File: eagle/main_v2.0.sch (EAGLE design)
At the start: 97 parts, among them IC1 74HC257D, IC2 PCA9530, IC3 RAC04, IC4 CS8416, IC5 MCP130-300I/SN, IC6 MAX1724, K1 G6A-234P, T1 BC847, T2 BC857, T3 BC847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

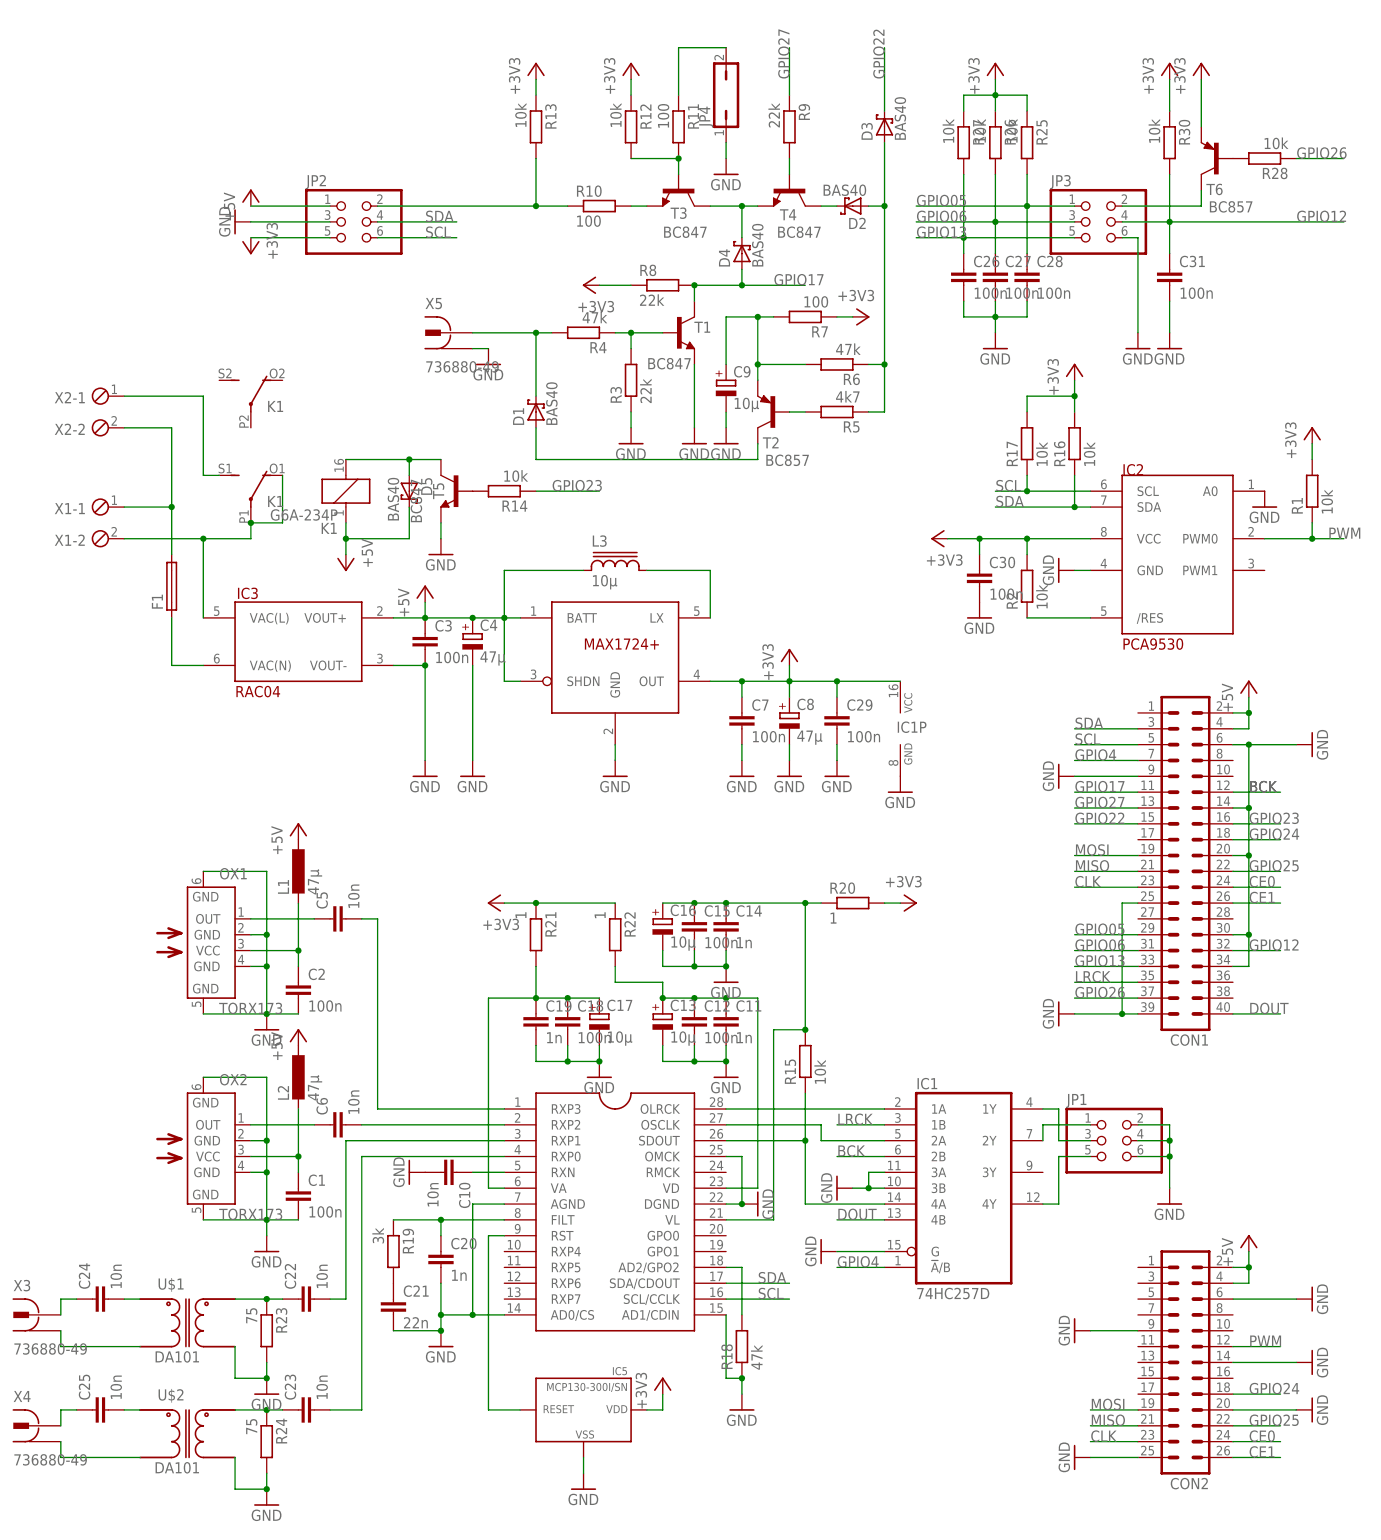
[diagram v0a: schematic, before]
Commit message: Eagle-Files: V2.0, zusätzlichen Ausgang für Relais eingebaut
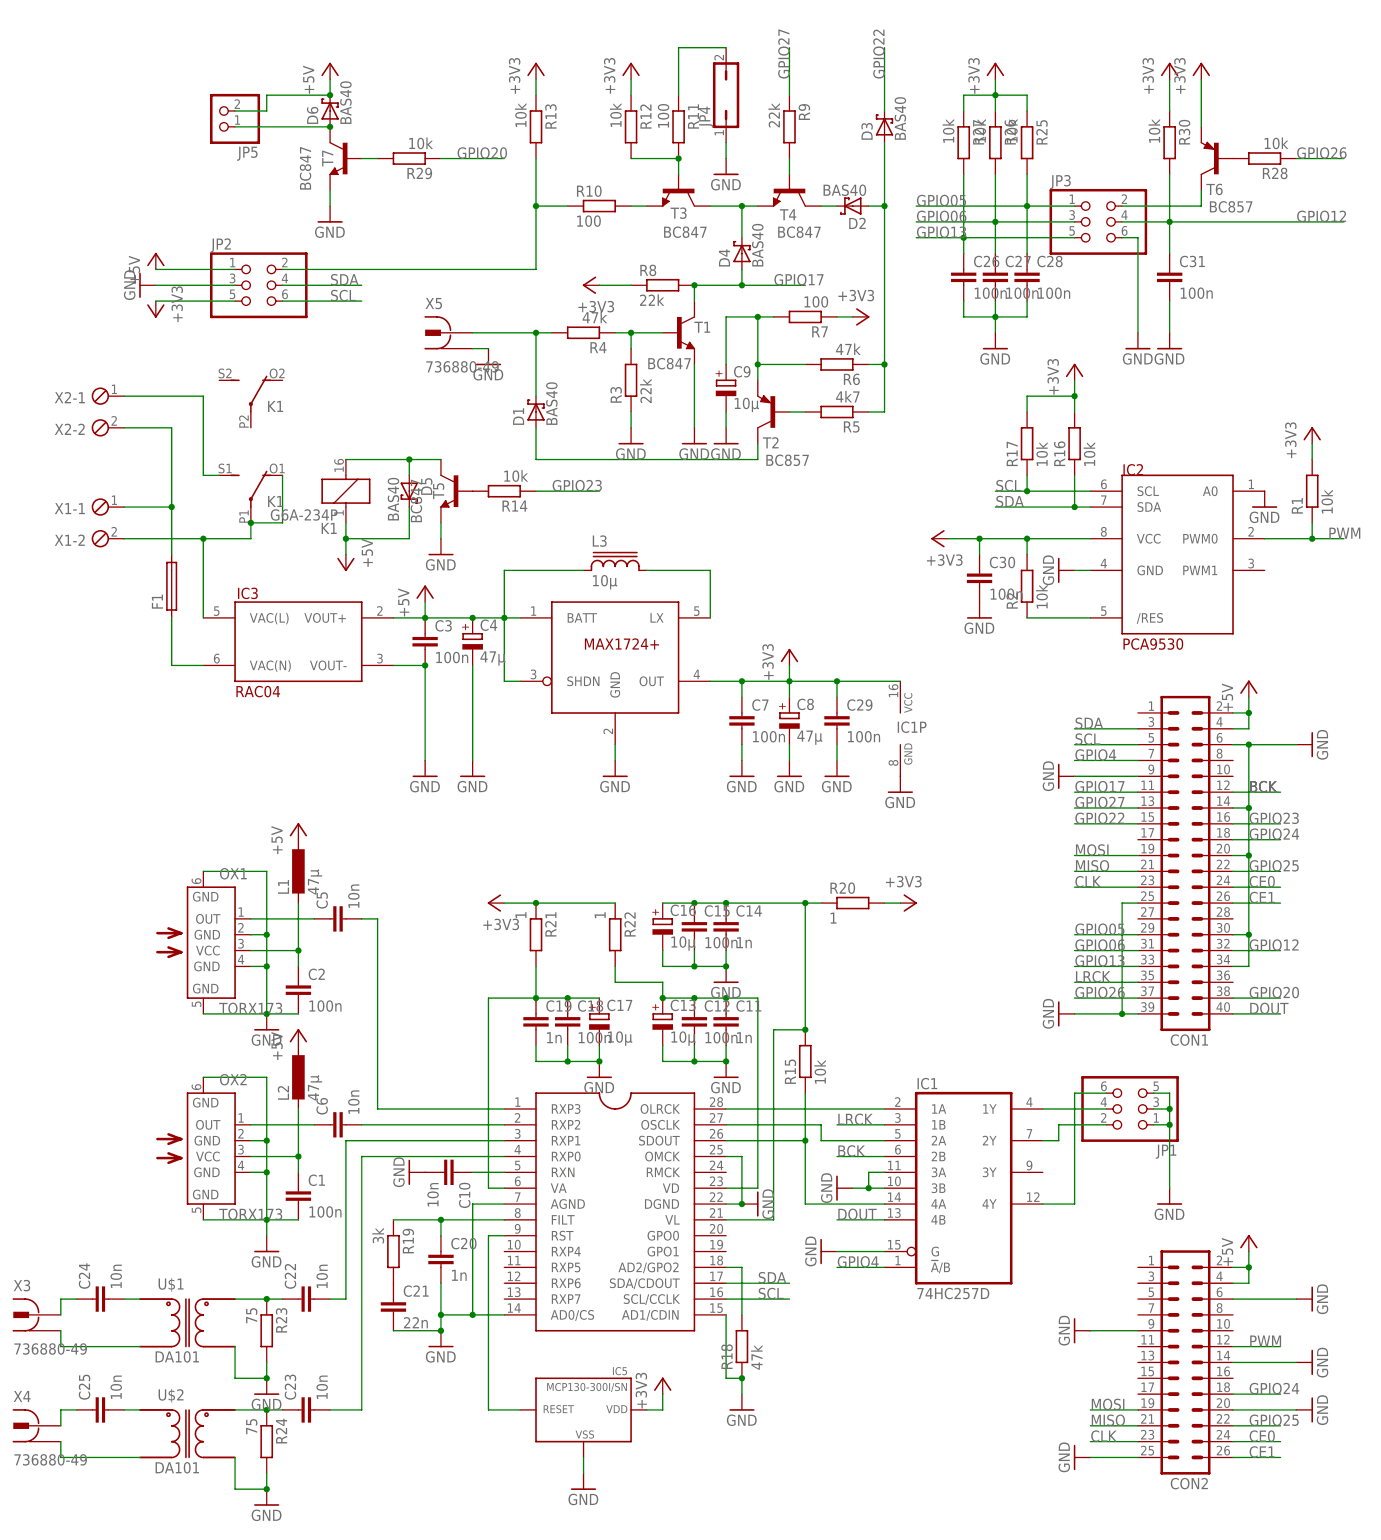
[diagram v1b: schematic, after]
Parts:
- added D6: BAS40, diode:BAS40
- added JP5: (no value), pinhead:PINHD-1X2
- added R29: 10k, rcl:R-EU_R0805
- added T7: BC847, transistor:BC847-NPN-SOT23-BEC
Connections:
- new net GPIO20: CON1.38, R29.1
- new net N$52: D6.A, JP5.1, T7.C
- new net N$55: R29.2, T7.B
- net +5V: now also D6.C, JP5.2
- net GND: now also JP1.1, JP1.3, JP1.5, T7.E; no longer JP1.2, JP1.4, JP1.6
- net N$26: now also JP1.2; no longer JP1.1
- net N$27: now also JP1.4; no longer JP1.3
- net N$53: now also JP1.6; no longer JP1.5
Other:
- moved on the sheet: JP1, JP2
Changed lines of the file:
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@@
 <part name="X5" library="con-conrad" deviceset="736880-49" device=""/>
 <part name="+3V15" library="supply1" deviceset="+3V3" device=""/>
+<part name="D6" library="diode" deviceset="BAS40" device=""/>
+<part name="T7" library="transistor" deviceset="*-NPN-" device="SOT23-BEC" technology="BC847" value="BC847"/>
+<part name="R29" library="rcl" deviceset="R-EU_" device="R0805" value="10k"/>
+<part name="GND44" library="supply1" deviceset="GND" device=""/>
+<part name="P+4" library="supply1" deviceset="+5V" device=""/>
+<part name="JP5" library="pinhead" deviceset="PINHD-1X2" device=""/>
 </parts>
 <sheets>
@@
 <attribute name="VALUE" x="88.9" y="172.72" size="1.778" layer="96"/>
 </instance>
-<instance part="JP1" gate="A" x="152.4" y="63.5"/>
+<instance part="JP1" gate="A" x="157.48" y="68.58" rot="R180"/>
 <instance part="GND15" gate="1" x="162.56" y="53.34"/>
 <instance part="T5" gate="G$1" x="48.26" y="167.64" smashed="yes" rot="MR0">
@@
 <instance part="F1" gate="F" x="2.54" y="152.4" rot="R90"/>
 <instance part="GND32" gate="1" x="53.34" y="187.96"/>
-<instance part="JP2" gate="A" x="30.48" y="210.82"/>
+<instance part="JP2" gate="A" x="15.24" y="200.66"/>
 <instance part="JP3" gate="A" x="149.86" y="210.82"/>
-<instance part="GND33" gate="1" x="12.7" y="210.82" rot="R270"/>
-<instance part="P+12" gate="1" x="15.24" y="215.9"/>
-<instance part="+3V7" gate="G$1" x="15.24" y="205.74" rot="R180"/>
+<instance part="GND33" gate="1" x="-2.54" y="200.66" rot="R270"/>
+<instance part="P+12" gate="1" x="0" y="205.74"/>
+<instance part="+3V7" gate="G$1" x="0" y="195.58" rot="R180"/>
 <instance part="GND34" gate="1" x="157.48" y="190.5"/>
 <instance part="R25" gate="G$1" x="139.7" y="223.52" rot="R270"/>
@@
 <instance part="X5" gate="G$1" x="48.26" y="193.04"/>
 <instance part="+3V15" gate="G$1" x="121.92" y="101.6" rot="R270"/>
+<instance part="D6" gate="1" x="27.94" y="228.6" rot="R90"/>
+<instance part="T7" gate="G$1" x="30.48" y="220.98" smashed="yes" rot="MR0">
+<attribute name="NAME" x="26.67" y="219.71" size="1.778" layer="95" rot="MR90"/>
+<attribute name="VALUE" x="24.892" y="223.012" size="1.778" layer="96" rot="MR270"/>
+</instance>
+<instance part="R29" gate="G$1" x="40.64" y="220.98" rot="R180"/>
+<instance part="GND44" gate="1" x="27.94" y="210.82"/>
+<instance part="P+4" gate="1" x="27.94" y="236.22"/>
+<instance part="JP5" gate="G$1" x="10.16" y="228.6" rot="R180"/>
 </instances>
 <busses>
@@
 <segment>
 <pinref part="JP2" gate="A" pin="4"/>
-<wire x1="35.56" y1="210.82" x2="48.26" y2="210.82" width="0.1524" layer="91"/>
-<label x="43.18" y="210.82" size="1.778" layer="95"/>
+<wire x1="20.32" y1="200.66" x2="33.02" y2="200.66" width="0.1524" layer="91"/>
+<label x="27.94" y="200.66" size="1.778" layer="95"/>
 </segment>
 </net>
@@
 <segment>
 <pinref part="JP2" gate="A" pin="6"/>
-<wire x1="35.56" y1="208.28" x2="48.26" y2="208.28" width="0.1524" layer="91"/>
-<label x="43.18" y="208.28" size="1.778" layer="95"/>
+<wire x1="20.32" y1="198.12" x2="33.02" y2="198.12" width="0.1524" layer="91"/>
+<label x="27.94" y="198.12" size="1.778" layer="95"/>
 </segment>
 </net>
@@
 </segment>
 <segment>
-<pinref part="JP1" gate="A" pin="2"/>
-<wire x1="157.48" y1="66.04" x2="162.56" y2="66.04" width="0.1524" layer="91"/>
-<wire x1="162.56" y1="66.04" x2="162.56" y2="63.5" width="0.1524" layer="91"/>
 <pinref part="GND15" gate="1" pin="GND"/>
-<pinref part="JP1" gate="A" pin="4"/>
-<wire x1="162.56" y1="63.5" x2="162.56" y2="60.96" width="0.1524" layer="91"/>
-<wire x1="162.56" y1="60.96" x2="162.56" y2="55.88" width="0.1524" layer="91"/>
-<wire x1="157.48" y1="63.5" x2="162.56" y2="63.5" width="0.1524" layer="91"/>
-<junction x="162.56" y="63.5"/>
-<pinref part="JP1" gate="A" pin="6"/>
-<wire x1="157.48" y1="60.96" x2="162.56" y2="60.96" width="0.1524" layer="91"/>
-<junction x="162.56" y="60.96"/>
+<pinref part="JP1" gate="A" pin="1"/>
+<pinref part="JP1" gate="A" pin="5"/>
+<wire x1="160.02" y1="71.12" x2="162.56" y2="71.12" width="0.1524" layer="91"/>
+<wire x1="162.56" y1="71.12" x2="162.56" y2="68.58" width="0.1524" layer="91"/>
+<pinref part="JP1" gate="A" pin="3"/>
+<wire x1="162.56" y1="68.58" x2="160.02" y2="68.58" width="0.1524" layer="91"/>
+<wire x1="162.56" y1="68.58" x2="162.56" y2="66.04" width="0.1524" layer="91"/>
+<junction x="162.56" y="68.58"/>
+<wire x1="162.56" y1="66.04" x2="160.02" y2="66.04" width="0.1524" layer="91"/>
+<wire x1="162.56" y1="66.04" x2="162.56" y2="55.88" width="0.1524" layer="91"/>
+<junction x="162.56" y="66.04"/>
 </segment>
 <segment>
@@
 <segment>
 <pinref part="JP2" gate="A" pin="3"/>
-<wire x1="27.94" y1="210.82" x2="15.24" y2="210.82" width="0.1524" layer="91"/>
+<wire x1="12.7" y1="200.66" x2="0" y2="200.66" width="0.1524" layer="91"/>
 <pinref part="GND33" gate="1" pin="GND"/>
 </segment>
@@
 <pinref part="CON2" gate="G$1" pin="25"/>
 <wire x1="149.86" y1="12.7" x2="157.48" y2="12.7" width="0.1524" layer="91"/>
+</segment>
+<segment>
+<pinref part="GND44" gate="1" pin="GND"/>
+<pinref part="T7" gate="G$1" pin="E"/>
+<wire x1="27.94" y1="213.36" x2="27.94" y2="215.9" width="0.1524" layer="91"/>
 </segment>
 </net>
@@
 <pinref part="P+12" gate="1" pin="+5V"/>
 <pinref part="JP2" gate="A" pin="1"/>
-<wire x1="15.24" y1="213.36" x2="27.94" y2="213.36" width="0.1524" layer="91"/>
+<wire x1="0" y1="203.2" x2="12.7" y2="203.2" width="0.1524" layer="91"/>
+</segment>
+<segment>
+<pinref part="D6" gate="1" pin="C"/>
+<pinref part="P+4" gate="1" pin="+5V"/>
+<wire x1="27.94" y1="231.14" x2="27.94" y2="233.68" width="0.1524" layer="91"/>
+<pinref part="JP5" gate="G$1" pin="2"/>
+<wire x1="12.7" y1="228.6" x2="17.78" y2="228.6" width="0.1524" layer="91"/>
+<wire x1="17.78" y1="228.6" x2="17.78" y2="231.14" width="0.1524" layer="91"/>
+<wire x1="17.78" y1="231.14" x2="27.94" y2="231.14" width="0.1524" layer="91"/>
+<junction x="27.94" y="231.14"/>
 </segment>
 </net>
@@
 <segment>
 <pinref part="JP2" gate="A" pin="5"/>
-<wire x1="27.94" y1="208.28" x2="15.24" y2="208.28" width="0.1524" layer="91"/>
+<wire x1="12.7" y1="198.12" x2="0" y2="198.12" width="0.1524" layer="91"/>
 <pinref part="+3V7" gate="G$1" pin="+3V3"/>
 </segment>
@@
 <wire x1="60.96" y1="213.36" x2="66.04" y2="213.36" width="0.1524" layer="91"/>
 <pinref part="JP2" gate="A" pin="2"/>
-<wire x1="35.56" y1="213.36" x2="60.96" y2="213.36" width="0.1524" layer="91"/>
 <junction x="60.96" y="213.36"/>
+<wire x1="60.96" y1="213.36" x2="60.96" y2="203.2" width="0.1524" layer="91"/>
+<wire x1="60.96" y1="203.2" x2="20.32" y2="203.2" width="0.1524" layer="91"/>
 </segment>
 </net>
@@
 <segment>
 <pinref part="IC1" gate="A" pin="2Y"/>
-<wire x1="142.24" y1="63.5" x2="142.24" y2="66.04" width="0.1524" layer="91"/>
-<pinref part="JP1" gate="A" pin="1"/>
-<wire x1="142.24" y1="66.04" x2="149.86" y2="66.04" width="0.1524" layer="91"/>
+<pinref part="JP1" gate="A" pin="2"/>
+<wire x1="144.78" y1="66.04" x2="152.4" y2="66.04" width="0.1524" layer="91"/>
+<wire x1="144.78" y1="66.04" x2="144.78" y2="63.5" width="0.1524" layer="91"/>
+<wire x1="144.78" y1="63.5" x2="142.24" y2="63.5" width="0.1524" layer="91"/>
 </segment>
 </net>
 <net name="N$27" class="0">
 <segment>
-<pinref part="JP1" gate="A" pin="3"/>
-<wire x1="149.86" y1="63.5" x2="144.78" y2="63.5" width="0.1524" layer="91"/>
-<wire x1="144.78" y1="63.5" x2="144.78" y2="68.58" width="0.1524" layer="91"/>
 <pinref part="IC1" gate="A" pin="1Y"/>
-<wire x1="144.78" y1="68.58" x2="142.24" y2="68.58" width="0.1524" layer="91"/>
+<pinref part="JP1" gate="A" pin="4"/>
+<wire x1="142.24" y1="68.58" x2="152.4" y2="68.58" width="0.1524" layer="91"/>
 </segment>
 </net>
@@
 <segment>
 <pinref part="IC1" gate="A" pin="4Y"/>
-<wire x1="142.24" y1="53.34" x2="144.78" y2="53.34" width="0.1524" layer="91"/>
-<wire x1="144.78" y1="53.34" x2="144.78" y2="60.96" width="0.1524" layer="91"/>
-<pinref part="JP1" gate="A" pin="5"/>
-<wire x1="144.78" y1="60.96" x2="149.86" y2="60.96" width="0.1524" layer="91"/>
+<pinref part="JP1" gate="A" pin="6"/>
+<wire x1="147.32" y1="53.34" x2="142.24" y2="53.34" width="0.1524" layer="91"/>
+<wire x1="147.32" y1="53.34" x2="147.32" y2="71.12" width="0.1524" layer="91"/>
+<wire x1="147.32" y1="71.12" x2="152.4" y2="71.12" width="0.1524" layer="91"/>
 </segment>
 </net>
@@
 </segment>
 </net>
+<net name="N$52" class="0">
+<segment>
+<pinref part="T7" gate="G$1" pin="C"/>
+<pinref part="D6" gate="1" pin="A"/>
+<pinref part="JP5" gate="G$1" pin="1"/>
+<wire x1="12.7" y1="226.06" x2="27.94" y2="226.06" width="0.1524" layer="91"/>
+<junction x="27.94" y="226.06"/>
+</segment>
+</net>
+<net name="N$55" class="0">
+<segment>
+<pinref part="T7" gate="G$1" pin="B"/>
+<pinref part="R29" gate="G$1" pin="2"/>
+<wire x1="33.02" y1="220.98" x2="35.56" y2="220.98" width="0.1524" layer="91"/>
+</segment>
+</net>
+<net name="GPIO20" class="0">
+<segment>
+<pinref part="CON1" gate="G$1" pin="38"/>
+<wire x1="172.72" y1="86.36" x2="180.34" y2="86.36" width="0.1524" layer="91"/>
+<label x="175.26" y="86.36" size="1.778" layer="95"/>
+</segment>
+<segment>
+<pinref part="R29" gate="G$1" pin="1"/>
+<wire x1="45.72" y1="220.98" x2="55.88" y2="220.98" width="0.1524" layer="91"/>
+<label x="48.26" y="220.98" size="1.778" layer="95"/>
+</segment>
+</net>
